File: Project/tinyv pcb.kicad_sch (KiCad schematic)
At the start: 102 parts, among them J1 JST SH, J2 Pico EZmate, J3 Conn_01x03_Socket, J5 Conn_01x09_Socket, J6 Conn_01x09_Socket, Q1 2N7002, SW1 RST, U1 MCP1700x-330xxTT, U3 STM32F072C8Tx

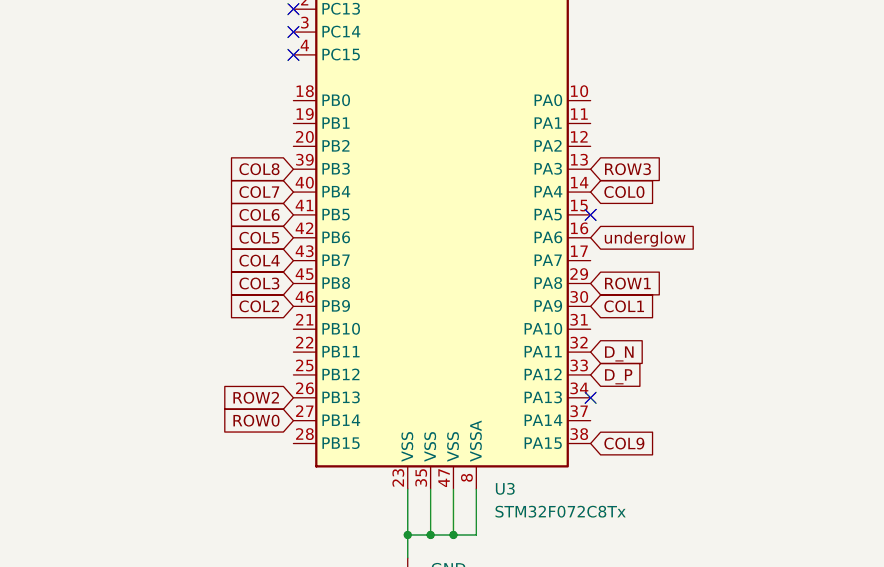
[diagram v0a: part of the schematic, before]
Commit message: added a version that uses FFC instead of JST
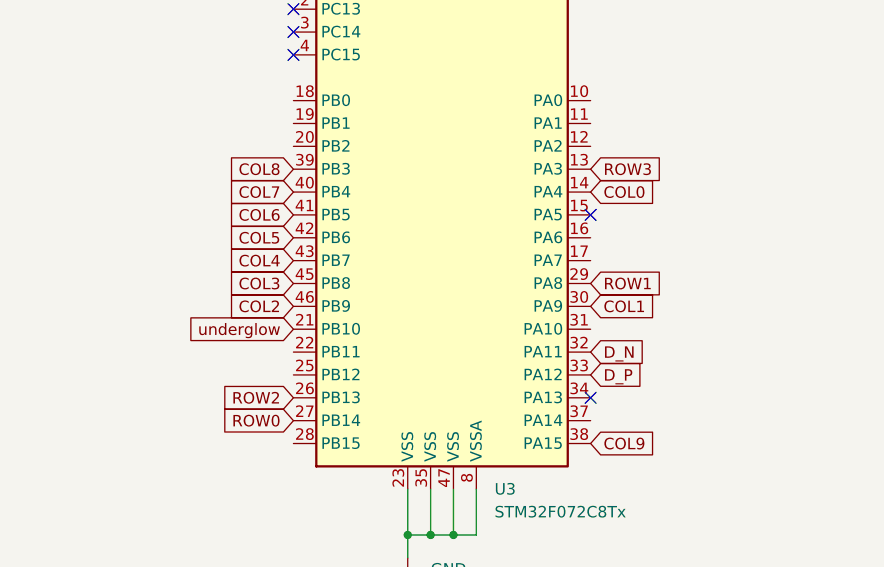
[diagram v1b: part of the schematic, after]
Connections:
- net underglow: now also U3.21 (PB10); no longer U3.16 (PA6)
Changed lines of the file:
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@@
     )
   )
-  (global_label "underglow" (shape input) (at 256.54 76.2 0) (fields_autoplaced)
-    (effects (font (size 1.27 1.27)) (justify left))
-    (property "Intersheetrefs" "${INTERSHEET_REFS}" (at 269.0613 76.2 0)
-      (effects (font (size 1.27 1.27)) (justify left) hide)
+  (global_label "underglow" (shape input) (at 223.52 86.36 180) (fields_autoplaced)
+    (effects (font (size 1.27 1.27)) (justify right))
+    (property "Intersheetrefs" "${INTERSHEET_REFS}" (at 210.9987 86.36 0)
+      (effects (font (size 1.27 1.27)) (justify right) hide)
     )
   )

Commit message: fresh gerbers
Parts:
- removed J5, J6: Conn_01x09_Socket, Connector_JST:JST_SH_SM09B-SRSS-TB_1x09-1MP_P1.00mm_Horizontal, symbol Connector:Conn_01x09_Socket
- added J4, J7: Conn_01x10_Socket, Connector_FFC-FPC:Hirose_FH12-10S-0.5SH_1x10-1MP_P0.50mm_Horizontal, symbol Connector:Conn_01x10_Socket
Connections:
- net COL5: now also J4.7 (Pin_7), J7.4 (Pin_4)
- net COL6: now also J4.6 (Pin_6), J7.5 (Pin_5)
- net COL7: now also J4.5 (Pin_5), J7.6 (Pin_6)
- net COL8: now also J4.4 (Pin_4), J7.7 (Pin_7)
- net COL9: now also J4.3 (Pin_3), J7.8 (Pin_8)
- net ROW0: now also J4.1 (Pin_1), J7.10 (Pin_10)
- net ROW1: now also J4.2 (Pin_2), J7.9 (Pin_9)
- net ROW2: now also J4.10 (Pin_10), J7.1 (Pin_1)
- net ROW3: now also J4.9 (Pin_9), J7.2 (Pin_2)
- net underglow: now also U3.17 (PA7); no longer U3.21 (PB10)
- no-connect marks 5 -> 21
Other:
- note added: "Hirose FFC connectors for the two pcb halves"
- note removed: "JST connectors for the two pcb halves"
